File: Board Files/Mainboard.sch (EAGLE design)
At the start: 115 parts, among them J1 I2C Display

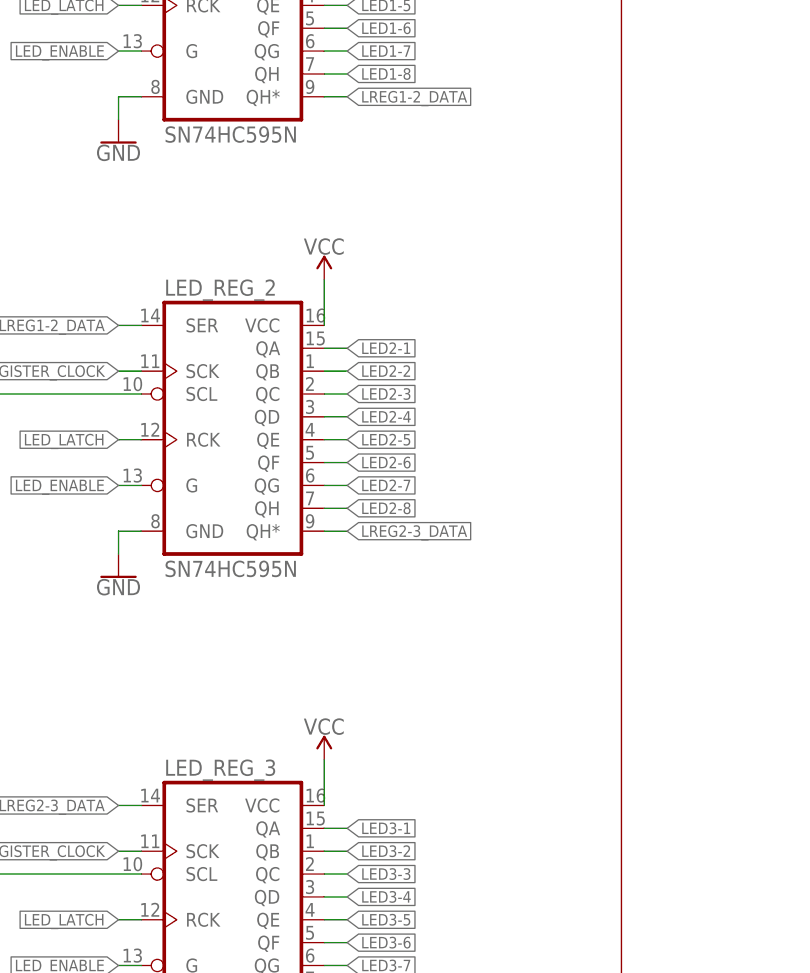
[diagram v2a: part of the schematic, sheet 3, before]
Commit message: Updated BRD and SCH
-Added more smoothing caps to schematic, placed things, reverted to old STL files
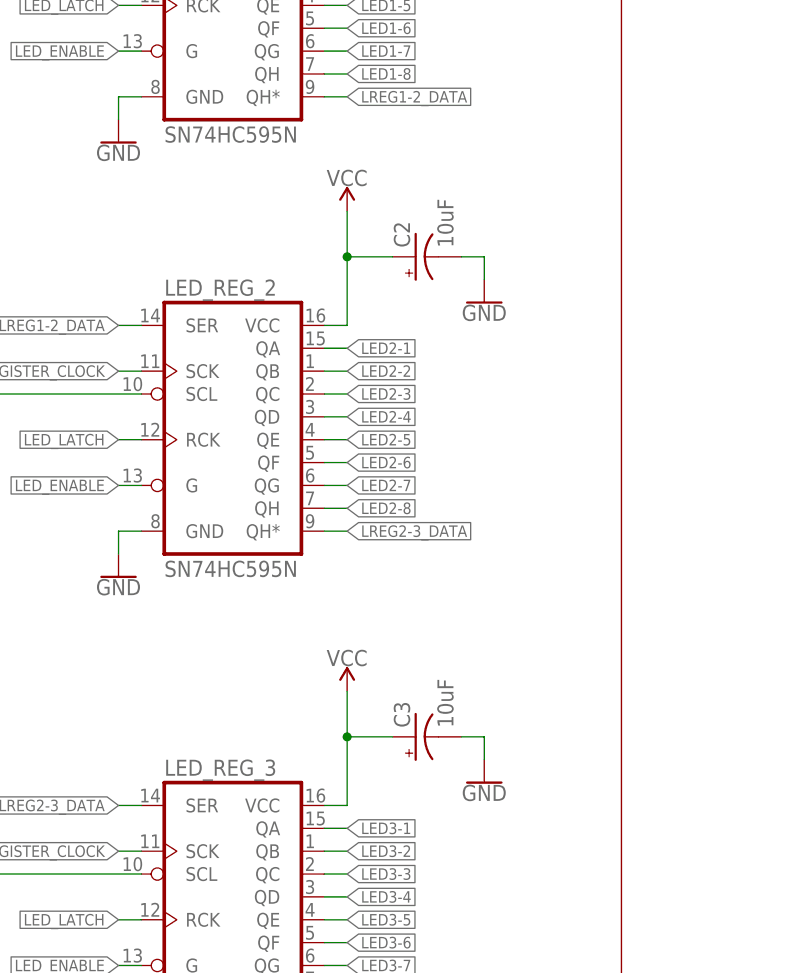
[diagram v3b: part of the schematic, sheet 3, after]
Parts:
- added C2, C3: 10uF, SparkFun-Capacitors:10UF-POLAR-RADIAL-2.5MM-25V-20%
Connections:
- net GND: now also C2.-, C3.-
- net VCC: now also C2.+, C3.+
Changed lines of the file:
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@@
 <part name="GND26" library="SparkFun-PowerSymbols" library_urn="urn:adsk.eagle:library:530" deviceset="GND" device=""/>
 <part name="LED_REG_2" library="SparkFun-IC-Logic" library_urn="urn:adsk.eagle:library:523" deviceset="74*595" device="N" package3d_urn="urn:adsk.eagle:package:38809/1" technology="HC" value="SN74HC595N "/>
-<part name="+5V25" library="SparkFun-PowerSymbols" library_urn="urn:adsk.eagle:library:530" deviceset="VCC" device=""/>
 <part name="LED_REG_3" library="SparkFun-IC-Logic" library_urn="urn:adsk.eagle:library:523" deviceset="74*595" device="N" package3d_urn="urn:adsk.eagle:package:38809/1" technology="HC" value="SN74HC595N "/>
-<part name="+5V26" library="SparkFun-PowerSymbols" library_urn="urn:adsk.eagle:library:530" deviceset="VCC" device=""/>
 <part name="KEY_REG_1" library="40xx" library_urn="urn:adsk.eagle:library:80" deviceset="4021" device="N" package3d_urn="urn:adsk.eagle:package:922/2"/>
 <part name="+5V31" library="SparkFun-PowerSymbols" library_urn="urn:adsk.eagle:library:530" deviceset="VCC" device=""/>
@@
 <part name="+5V41" library="SparkFun-PowerSymbols" library_urn="urn:adsk.eagle:library:530" deviceset="VCC" device=""/>
 <part name="VR1" library="SparkFun-Resistors" library_urn="urn:adsk.eagle:library:532" deviceset="POTENTIOMETER" device="-PTH-9MM-1/20W-20%" package3d_urn="urn:adsk.eagle:package:39672/1" value="10k"/>
+<part name="C2" library="SparkFun-Capacitors" library_urn="urn:adsk.eagle:library:510" deviceset="10UF-POLAR" device="-RADIAL-2.5MM-25V-20%" package3d_urn="urn:adsk.eagle:package:37423/1" value="10uF"/>
+<part name="+5V25" library="SparkFun-PowerSymbols" library_urn="urn:adsk.eagle:library:530" deviceset="VCC" device=""/>
+<part name="GND38" library="SparkFun-PowerSymbols" library_urn="urn:adsk.eagle:library:530" deviceset="GND" device=""/>
+<part name="C3" library="SparkFun-Capacitors" library_urn="urn:adsk.eagle:library:510" deviceset="10UF-POLAR" device="-RADIAL-2.5MM-25V-20%" package3d_urn="urn:adsk.eagle:package:37423/1" value="10uF"/>
+<part name="+5V26" library="SparkFun-PowerSymbols" library_urn="urn:adsk.eagle:library:530" deviceset="VCC" device=""/>
+<part name="GND39" library="SparkFun-PowerSymbols" library_urn="urn:adsk.eagle:library:530" deviceset="GND" device=""/>
 </parts>
 <sheets>
@@
 <attribute name="VALUE" x="86.36" y="111.76" size="1.778" layer="95" font="vector"/>
 </instance>
-<instance part="+5V25" gate="G$1" x="104.14" y="144.78" smashed="yes">
-<attribute name="VALUE" x="104.14" y="147.574" size="1.778" layer="96" align="bottom-center"/>
-</instance>
 <instance part="LED_REG_3" gate="U1" x="91.44" y="76.2" smashed="yes">
 <attribute name="NAME" x="86.36" y="89.662" size="1.778" layer="95" font="vector"/>
 <attribute name="VALUE" x="86.36" y="58.42" size="1.778" layer="95" font="vector"/>
 </instance>
-<instance part="+5V26" gate="G$1" x="104.14" y="91.44" smashed="yes">
-<attribute name="VALUE" x="104.14" y="94.234" size="1.778" layer="96" align="bottom-center"/>
-</instance>
 <instance part="KEY_REG_1" gate="A" x="261.62" y="182.88" smashed="yes">
 <attribute name="NAME" x="254" y="201.295" size="1.778" layer="95"/>
@@
 <instance part="GND30" gate="1" x="81.28" y="58.42" smashed="yes">
 <attribute name="VALUE" x="81.28" y="58.166" size="1.778" layer="96" align="top-center"/>
+</instance>
+<instance part="C2" gate="G$1" x="114.3" y="147.32" smashed="yes" rot="R90">
+<attribute name="NAME" x="113.665" y="148.336" size="1.778" layer="95" font="vector" rot="R90"/>
+<attribute name="VALUE" x="118.491" y="148.336" size="1.778" layer="96" font="vector" rot="R90"/>
+</instance>
+<instance part="+5V25" gate="G$1" x="106.68" y="152.4" smashed="yes">
+<attribute name="VALUE" x="106.68" y="155.194" size="1.778" layer="96" align="bottom-center"/>
+</instance>
+<instance part="GND38" gate="1" x="121.92" y="142.24" smashed="yes">
+<attribute name="VALUE" x="121.92" y="141.986" size="1.778" layer="96" align="top-center"/>
+</instance>
+<instance part="C3" gate="G$1" x="114.3" y="93.98" smashed="yes" rot="R90">
+<attribute name="NAME" x="113.665" y="94.996" size="1.778" layer="95" font="vector" rot="R90"/>
+<attribute name="VALUE" x="118.491" y="94.996" size="1.778" layer="96" font="vector" rot="R90"/>
+</instance>
+<instance part="+5V26" gate="G$1" x="106.68" y="99.06" smashed="yes">
+<attribute name="VALUE" x="106.68" y="101.854" size="1.778" layer="96" align="bottom-center"/>
+</instance>
+<instance part="GND39" gate="1" x="121.92" y="88.9" smashed="yes">
+<attribute name="VALUE" x="121.92" y="88.646" size="1.778" layer="96" align="top-center"/>
 </instance>
 </instances>
@@
 </segment>
 <segment>
-<pinref part="+5V25" gate="G$1" pin="VCC"/>
-<pinref part="LED_REG_2" gate="U1" pin="VCC"/>
-<wire x1="104.14" y1="139.7" x2="104.14" y2="144.78" width="0.1524" layer="91"/>
-</segment>
-<segment>
-<pinref part="+5V26" gate="G$1" pin="VCC"/>
-<pinref part="LED_REG_3" gate="U1" pin="VCC"/>
-<wire x1="104.14" y1="86.36" x2="104.14" y2="91.44" width="0.1524" layer="91"/>
-</segment>
-<segment>
 <pinref part="+5V31" gate="G$1" pin="VCC"/>
 <pinref part="KEY_REG_1" gate="P" pin="VDD"/>
@@
 <pinref part="LED_REG_3" gate="U1" pin="SCL"/>
 </segment>
+<segment>
+<pinref part="+5V25" gate="G$1" pin="VCC"/>
+<wire x1="106.68" y1="147.32" x2="111.76" y2="147.32" width="0.1524" layer="91"/>
+<pinref part="C2" gate="G$1" pin="+"/>
+<wire x1="106.68" y1="152.4" x2="106.68" y2="147.32" width="0.1524" layer="91"/>
+<wire x1="106.68" y1="147.32" x2="106.68" y2="139.7" width="0.1524" layer="91"/>
+<junction x="106.68" y="147.32"/>
+<pinref part="LED_REG_2" gate="U1" pin="VCC"/>
+<wire x1="106.68" y1="139.7" x2="104.14" y2="139.7" width="0.1524" layer="91"/>
+</segment>
+<segment>
+<pinref part="+5V26" gate="G$1" pin="VCC"/>
+<wire x1="106.68" y1="93.98" x2="111.76" y2="93.98" width="0.1524" layer="91"/>
+<pinref part="C3" gate="G$1" pin="+"/>
+<wire x1="106.68" y1="99.06" x2="106.68" y2="93.98" width="0.1524" layer="91"/>
+<wire x1="106.68" y1="93.98" x2="106.68" y2="86.36" width="0.1524" layer="91"/>
+<junction x="106.68" y="93.98"/>
+<pinref part="LED_REG_3" gate="U1" pin="VCC"/>
+<wire x1="104.14" y1="86.36" x2="106.68" y2="86.36" width="0.1524" layer="91"/>
+</segment>
 </net>
 <net name="GND" class="0">
@@
 <pinref part="LED_REG_3" gate="U1" pin="GND"/>
 </segment>
-</net>
+<segment>
+<pinref part="C2" gate="G$1" pin="-"/>
+<wire x1="119.38" y1="147.32" x2="121.92" y2="147.32" width="0.1524" layer="91"/>
+<pinref part="GND38" gate="1" pin="GND"/>
+<wire x1="121.92" y1="147.32" x2="121.92" y2="144.78" width="0.1524" layer="91"/>
+</segment>
+<segment>
+<pinref part="C3" gate="G$1" pin="-"/>
+<wire x1="119.38" y1="93.98" x2="121.92" y2="93.98" width="0.1524" layer="91"/>
+<pinref part="GND39" gate="1" pin="GND"/>
+<wire x1="121.92" y1="93.98" x2="121.92" y2="91.44" width="0.1524" layer="91"/>
+</segment>
+</net>

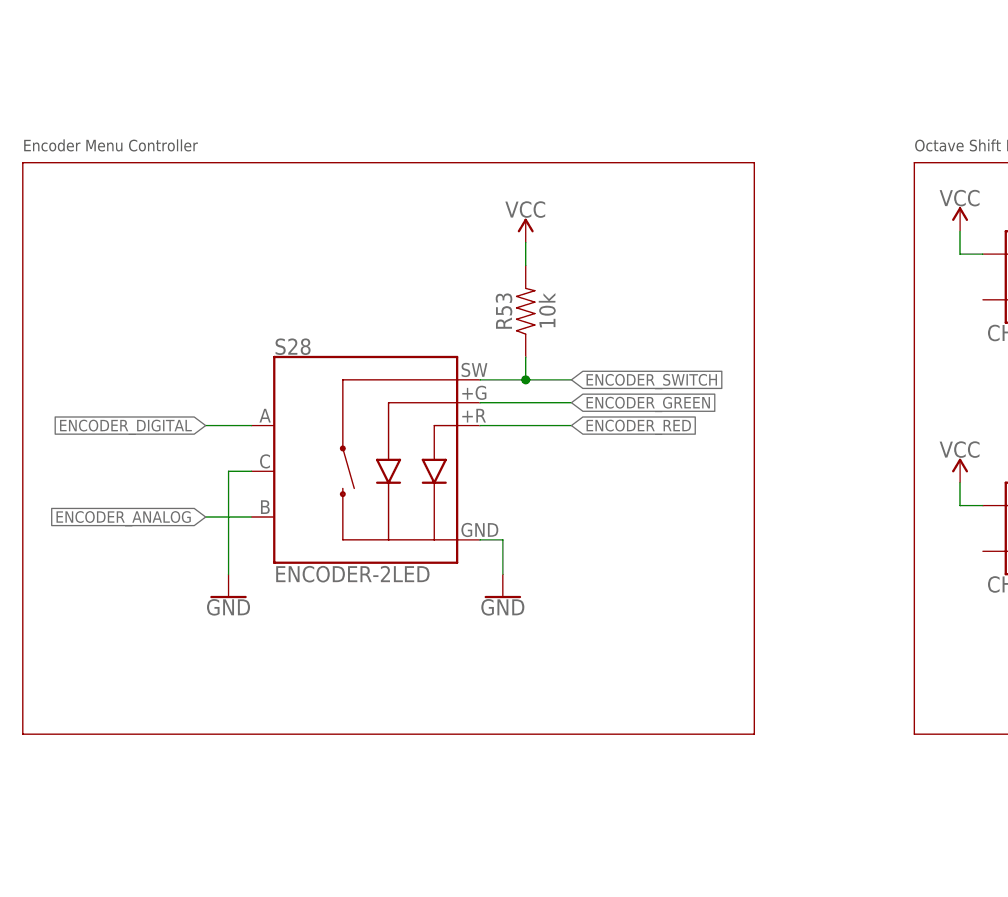
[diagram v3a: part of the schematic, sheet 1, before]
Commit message: Finished Manual Routing
Finished routing manual traces. Will autoroute the switch and LED traces
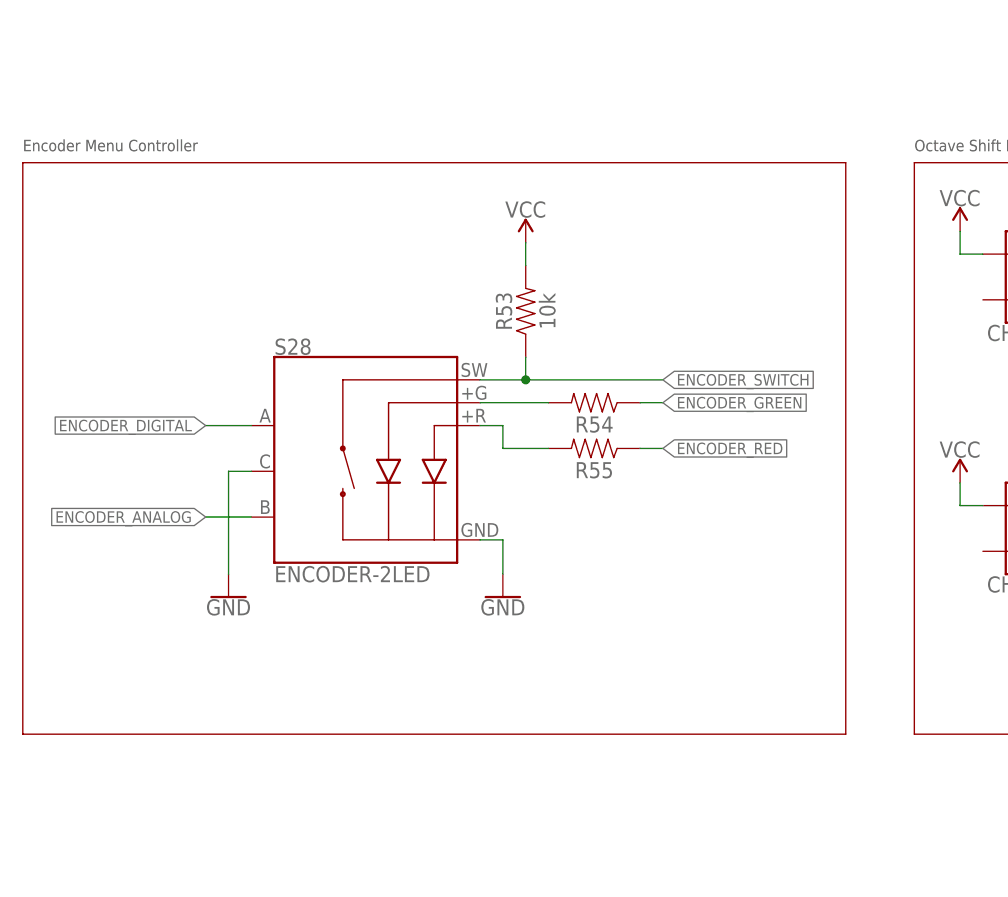
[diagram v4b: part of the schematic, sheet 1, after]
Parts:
- added R54, R55: (no value), SparkFun-Resistors:RESISTORAXIAL-0.3
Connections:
- removed net LED_ENABLE: LED_REG_1.G, LED_REG_2.G, LED_REG_3.G
- new net N$25: R54.2, S28.+G
- new net N$26: R55.2, S28.+R
- net ENCODER_GREEN: now also R54.1; no longer S28.+G
- net ENCODER_RED: now also R55.1; no longer S28.+R
- net LED_OUTPUT_EN: now also LED_REG_1.G, LED_REG_2.G, LED_REG_3.G
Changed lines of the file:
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@@
 <?xml version="1.0" encoding="utf-8"?>
 <!DOCTYPE eagle SYSTEM "eagle.dtd">
-<eagle version="9.3.1">
+<eagle version="9.3.0">
 <drawing>
 <settings>
-<setting alwaysvectorfont="yes"/>
+<setting alwaysvectorfont="no"/>
 <setting verticaltext="up"/>
 </settings>
@@
 <part name="+5V26" library="SparkFun-PowerSymbols" library_urn="urn:adsk.eagle:library:530" deviceset="VCC" device=""/>
 <part name="GND39" library="SparkFun-PowerSymbols" library_urn="urn:adsk.eagle:library:530" deviceset="GND" device=""/>
+<part name="R54" library="SparkFun-Resistors" library_urn="urn:adsk.eagle:library:532" deviceset="RESISTOR" device="AXIAL-0.3" package3d_urn="urn:adsk.eagle:package:39658/1" value=" "/>
+<part name="R55" library="SparkFun-Resistors" library_urn="urn:adsk.eagle:library:532" deviceset="RESISTOR" device="AXIAL-0.3" package3d_urn="urn:adsk.eagle:package:39658/1" value=" "/>
 </parts>
 <sheets>
@@
 <wire x1="119.38" y1="31.75" x2="119.38" y2="95.25" width="0.1524" layer="94"/>
 <text x="119.38" y="96.52" size="1.27" layer="97">Octave Shift Buttons</text>
-<wire x1="20.32" y1="95.25" x2="101.6" y2="95.25" width="0.1524" layer="94"/>
-<wire x1="101.6" y1="95.25" x2="101.6" y2="31.75" width="0.1524" layer="94"/>
-<wire x1="101.6" y1="31.75" x2="20.32" y2="31.75" width="0.1524" layer="94"/>
+<wire x1="20.32" y1="95.25" x2="111.76" y2="95.25" width="0.1524" layer="94"/>
+<wire x1="111.76" y1="95.25" x2="111.76" y2="31.75" width="0.1524" layer="94"/>
+<wire x1="111.76" y1="31.75" x2="20.32" y2="31.75" width="0.1524" layer="94"/>
 <wire x1="20.32" y1="31.75" x2="20.32" y2="95.25" width="0.1524" layer="94"/>
 <text x="20.32" y="96.52" size="1.27" layer="97">Encoder Menu Controller</text>
@@
 <attribute name="VALUE" x="200.66" y="107.95" size="1.778" layer="95" font="vector" rot="R180" align="bottom-center"/>
 </instance>
+<instance part="R54" gate="G$1" x="83.82" y="68.58" smashed="yes" rot="R180">
+<attribute name="NAME" x="83.82" y="67.056" size="1.778" layer="95" font="vector" rot="R180" align="bottom-center"/>
+<attribute name="VALUE" x="83.82" y="70.104" size="1.778" layer="96" font="vector" rot="R180" align="top-center"/>
+</instance>
+<instance part="R55" gate="G$1" x="83.82" y="63.5" smashed="yes" rot="R180">
+<attribute name="NAME" x="83.82" y="61.976" size="1.778" layer="95" font="vector" rot="R180" align="bottom-center"/>
+<attribute name="VALUE" x="83.82" y="65.024" size="1.778" layer="96" font="vector" rot="R180" align="top-center"/>
+</instance>
 </instances>
 <busses>
@@
 <pinref part="S28" gate="G$1" pin="SW"/>
 <wire x1="71.12" y1="71.12" x2="76.2" y2="71.12" width="0.1524" layer="91"/>
-<wire x1="76.2" y1="71.12" x2="81.28" y2="71.12" width="0.1524" layer="91"/>
+<wire x1="76.2" y1="71.12" x2="91.44" y2="71.12" width="0.1524" layer="91"/>
 <wire x1="76.2" y1="71.12" x2="76.2" y2="73.66" width="0.1524" layer="91"/>
 <junction x="76.2" y="71.12"/>
 <pinref part="R53" gate="G$1" pin="1"/>
-<label x="81.28" y="71.12" size="1.27" layer="95" xref="yes"/>
+<label x="91.44" y="71.12" size="1.27" layer="95" xref="yes"/>
 </segment>
 <segment>
@@
 </segment>
 <segment>
-<label x="81.28" y="68.58" size="1.27" layer="95" xref="yes"/>
-<pinref part="S28" gate="G$1" pin="+G"/>
-<wire x1="71.12" y1="68.58" x2="81.28" y2="68.58" width="0.1524" layer="91"/>
+<pinref part="R54" gate="G$1" pin="1"/>
+<wire x1="88.9" y1="68.58" x2="91.44" y2="68.58" width="0.1524" layer="91"/>
+<label x="91.44" y="68.58" size="1.27" layer="95" xref="yes"/>
 </segment>
 </net>
@@
 </segment>
 <segment>
-<label x="81.28" y="66.04" size="1.27" layer="95" xref="yes"/>
+<pinref part="R55" gate="G$1" pin="1"/>
+<wire x1="88.9" y1="63.5" x2="91.44" y2="63.5" width="0.1524" layer="91"/>
+<label x="91.44" y="63.5" size="1.27" layer="95" xref="yes"/>
+</segment>
+</net>
+<net name="N$25" class="0">
+<segment>
+<pinref part="S28" gate="G$1" pin="+G"/>
+<pinref part="R54" gate="G$1" pin="2"/>
+<wire x1="71.12" y1="68.58" x2="78.74" y2="68.58" width="0.1524" layer="91"/>
+</segment>
+</net>
+<net name="N$26" class="0">
+<segment>
 <pinref part="S28" gate="G$1" pin="+R"/>
-<wire x1="71.12" y1="66.04" x2="81.28" y2="66.04" width="0.1524" layer="91"/>
+<wire x1="71.12" y1="66.04" x2="73.66" y2="66.04" width="0.1524" layer="91"/>
+<wire x1="73.66" y1="66.04" x2="73.66" y2="63.5" width="0.1524" layer="91"/>
+<pinref part="R55" gate="G$1" pin="2"/>
+<wire x1="73.66" y1="63.5" x2="78.74" y2="63.5" width="0.1524" layer="91"/>
 </segment>
 </net>
@@
 </segment>
 </net>
-<net name="LED_ENABLE" class="0">
+<net name="LED_OUTPUT_EN" class="0">
 <segment>
 <pinref part="LED_REG_1" gate="U1" pin="G"/>

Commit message: Finished Mainboard V1.0
-Added holes
-Labeled everything
-Final trace cleanup
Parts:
- S5: value CHERRY_LED -> MOMENTARY-SWITCH-SPST-LED-PTH-CHERRY
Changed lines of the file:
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@@
 <part name="D4" library="SparkFun-LED" library_urn="urn:adsk.eagle:library:529" deviceset="LED" device="5MM" package3d_urn="urn:adsk.eagle:package:39353/1"/>
 <part name="R9" library="SparkFun-Resistors" library_urn="urn:adsk.eagle:library:532" deviceset="RESISTOR" device="AXIAL-0.3" package3d_urn="urn:adsk.eagle:package:39658/1" value=" "/>
-<part name="S5" library="SparkFun-Switches" library_urn="urn:adsk.eagle:library:535" deviceset="MOMENTARY-SWITCH-SPST-LED" device="-PTH-CHERRY" package3d_urn="urn:adsk.eagle:package:40173/1" value="CHERRY_LED"/>
+<part name="S5" library="SparkFun-Switches" library_urn="urn:adsk.eagle:library:535" deviceset="MOMENTARY-SWITCH-SPST-LED" device="-PTH-CHERRY" package3d_urn="urn:adsk.eagle:package:40173/1" value=""/>
 <part name="+5V4" library="SparkFun-PowerSymbols" library_urn="urn:adsk.eagle:library:530" deviceset="VCC" device=""/>
 <part name="R10" library="SparkFun-Resistors" library_urn="urn:adsk.eagle:library:532" deviceset="10KOHM" device="-HORIZ-1/4W-1%" package3d_urn="urn:adsk.eagle:package:39658/1" value="10k"/>
